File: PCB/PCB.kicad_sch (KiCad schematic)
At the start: 37 parts, among them SW1 SW_Push, SW10 SW_Push, SW11 SW_Push, SW12 SW_Push, SW13 SW_Push, SW14 SW_Push, SW15 SW_Push, SW16 SW_Push, SW17 RotaryEncoder_Switch, SW18 RotaryEncoder_Switch, SW2 SW_Push, SW3 SW_Push, SW4 SW_Push, SW5 SW_Push, SW6 SW_Push, SW7 SW_Push, SW8 SW_Push, SW9 SW_Push, U1 RP2040-Zero

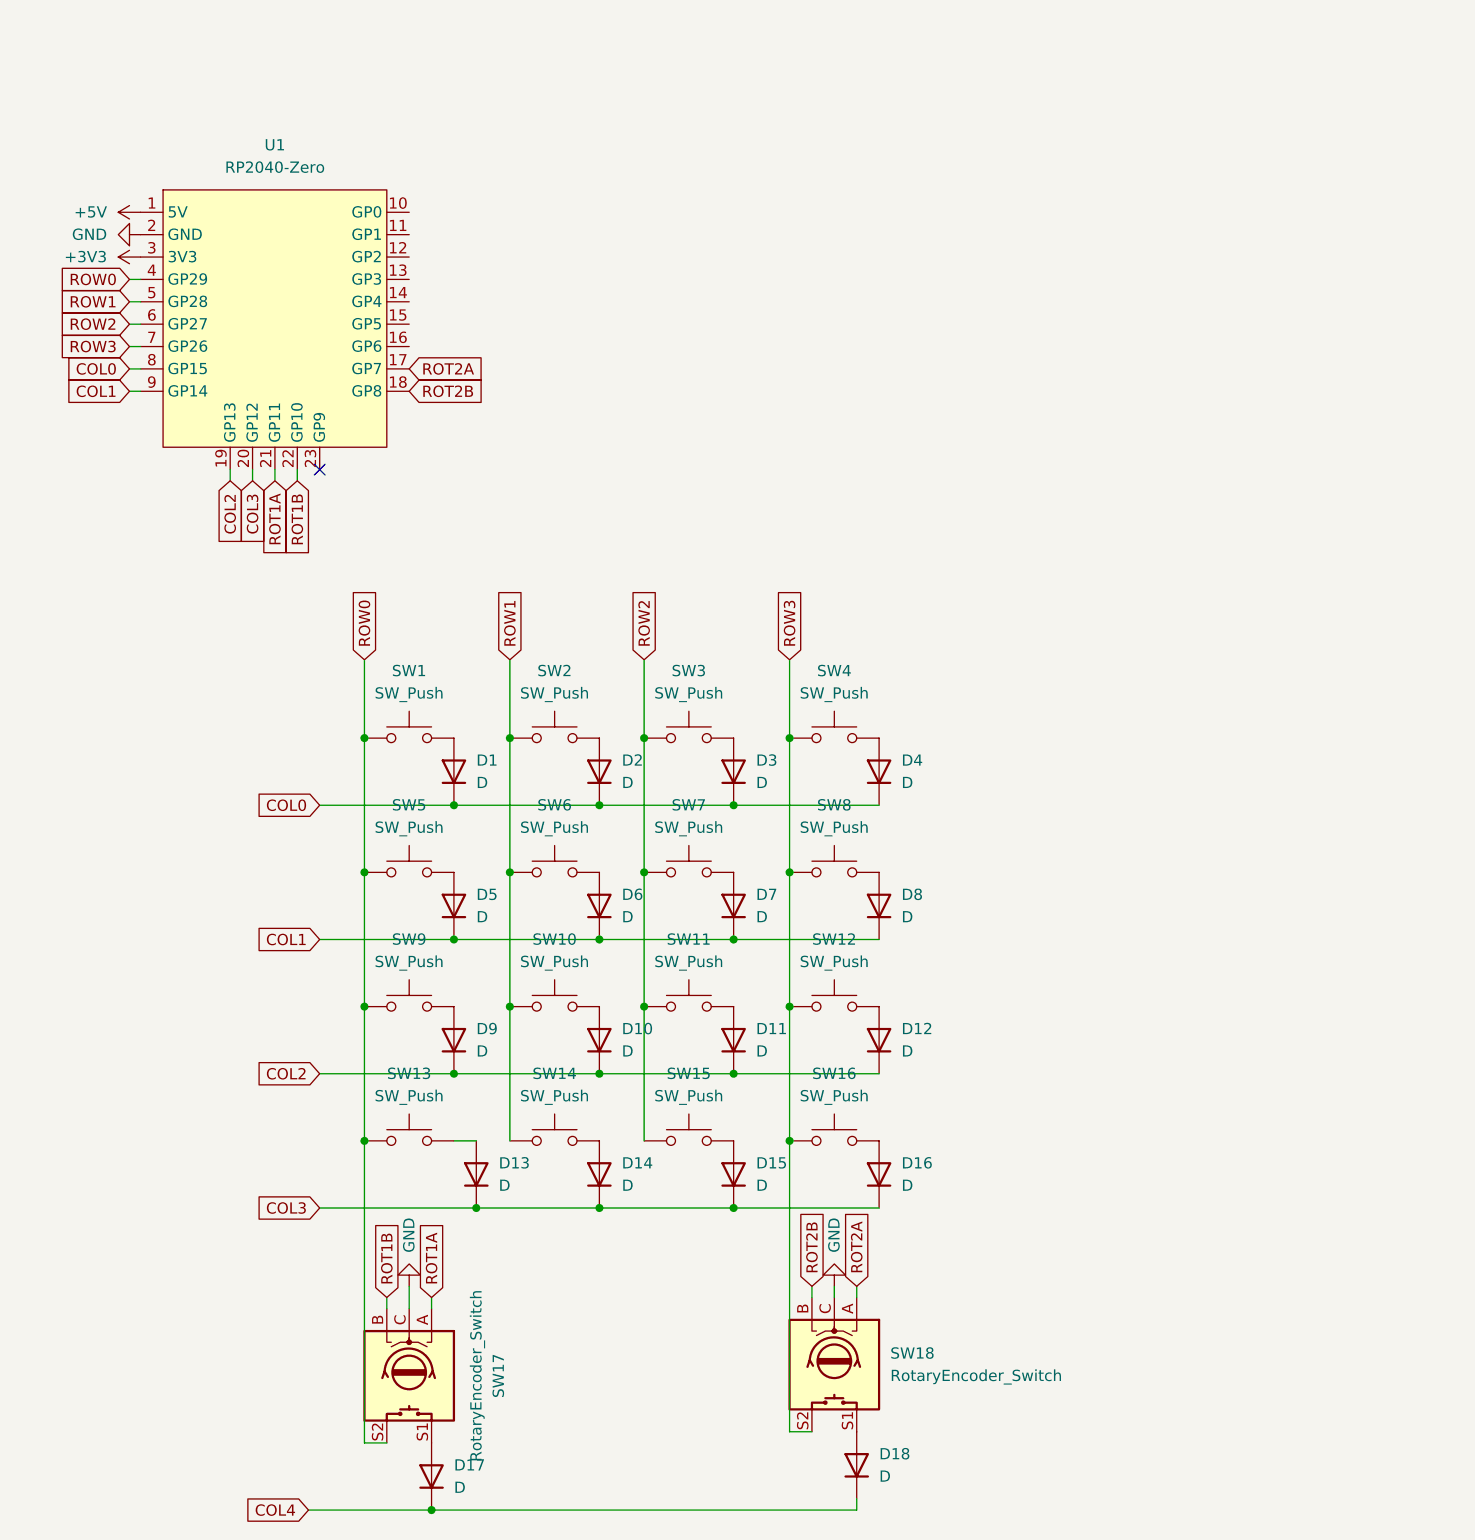
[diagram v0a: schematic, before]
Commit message: Added /Images
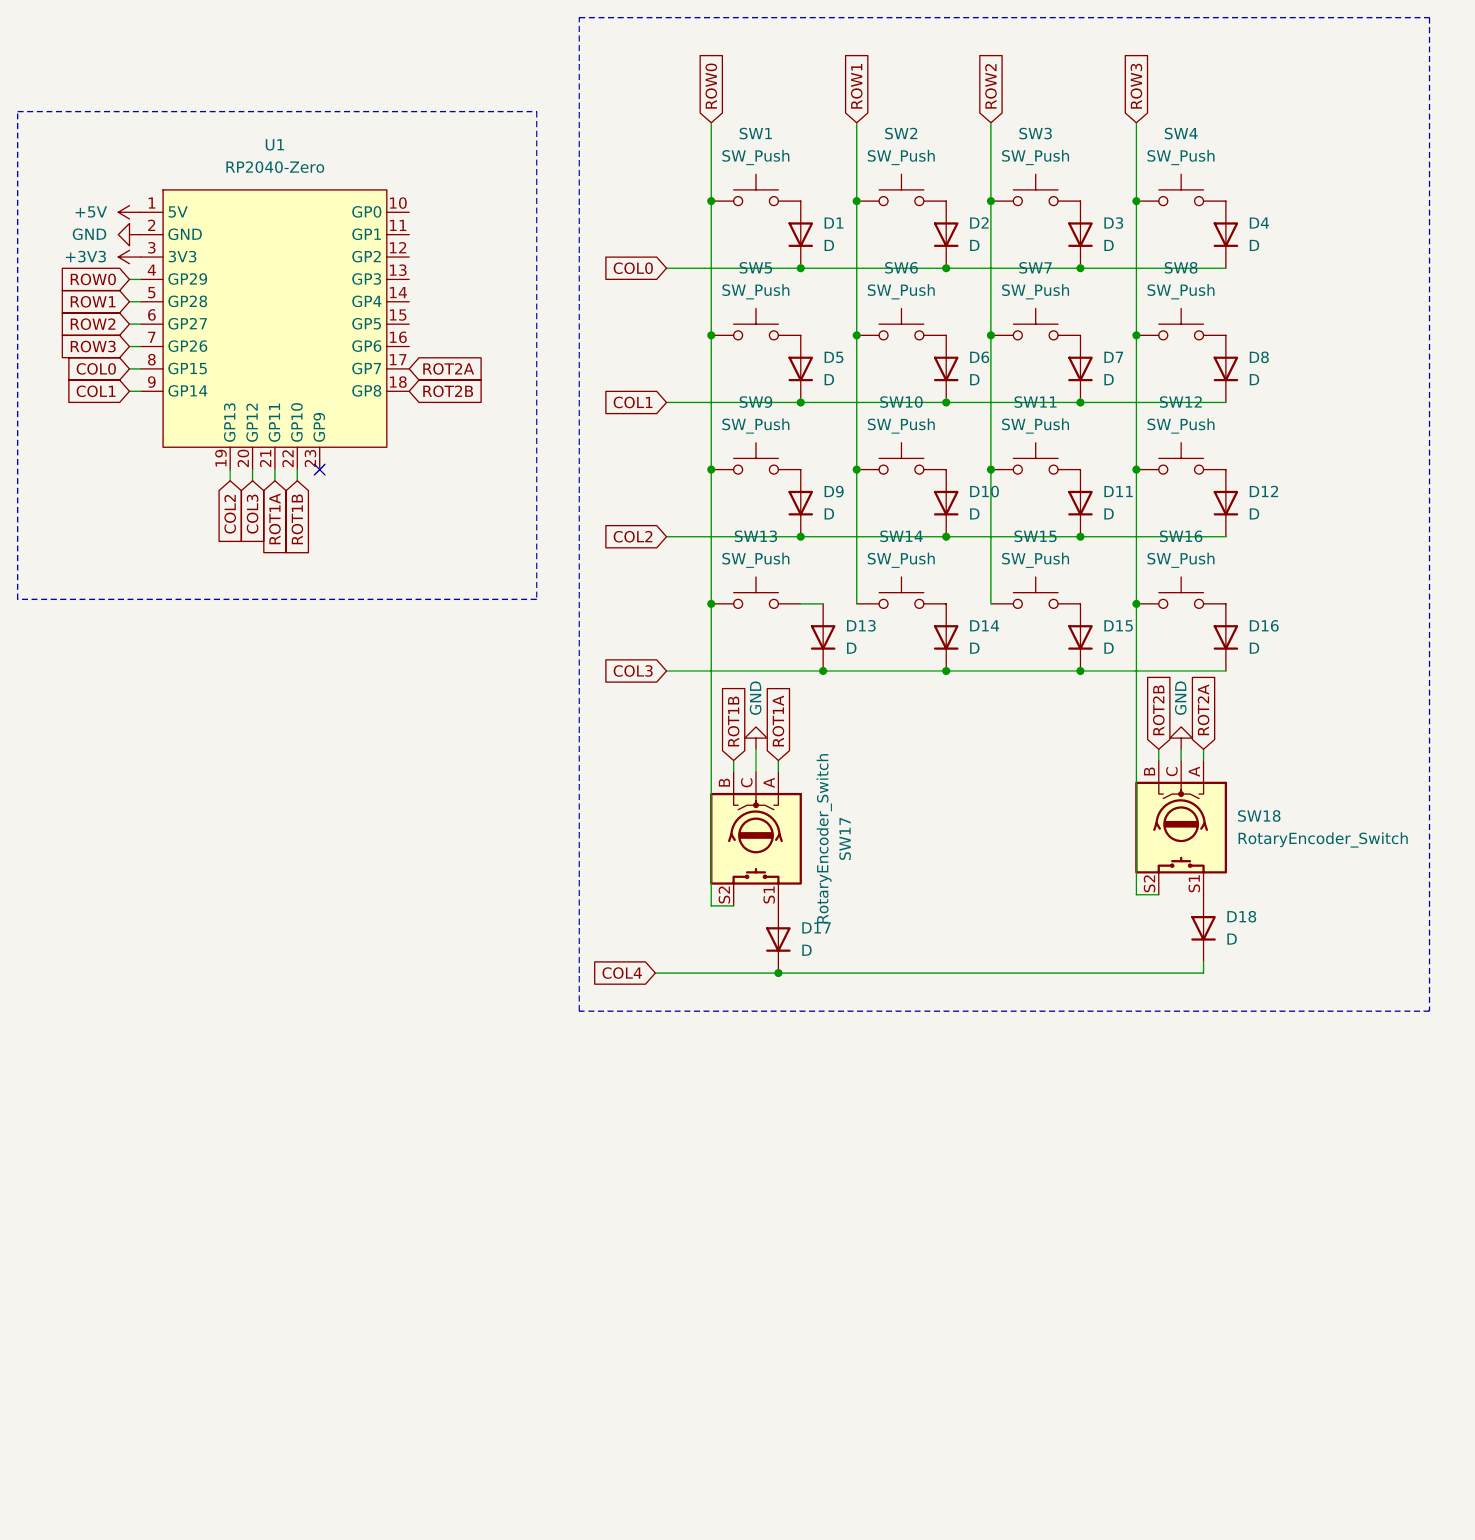
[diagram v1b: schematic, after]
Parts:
- SW1, SW10, SW11, SW12, SW13, SW14, SW15, SW16, SW2, SW3, SW4, SW5, SW6, SW7, SW8, SW9: footprint Taps Keyboard shit:SW_Cherry_MX_1.00u_PCB -> KEYS:SW_Hotswap_Kailh_MX
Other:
- moved on the sheet: D1, D10, D11, D12, D13, D14, D15, D16, D17, D18, D2, D3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
